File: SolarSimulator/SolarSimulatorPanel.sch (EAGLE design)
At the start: 82 parts, among them U1 Red Driver, U2 LM3404HVMA, U3 Blue Driver, X1 MKDSN1,5/2-5,08

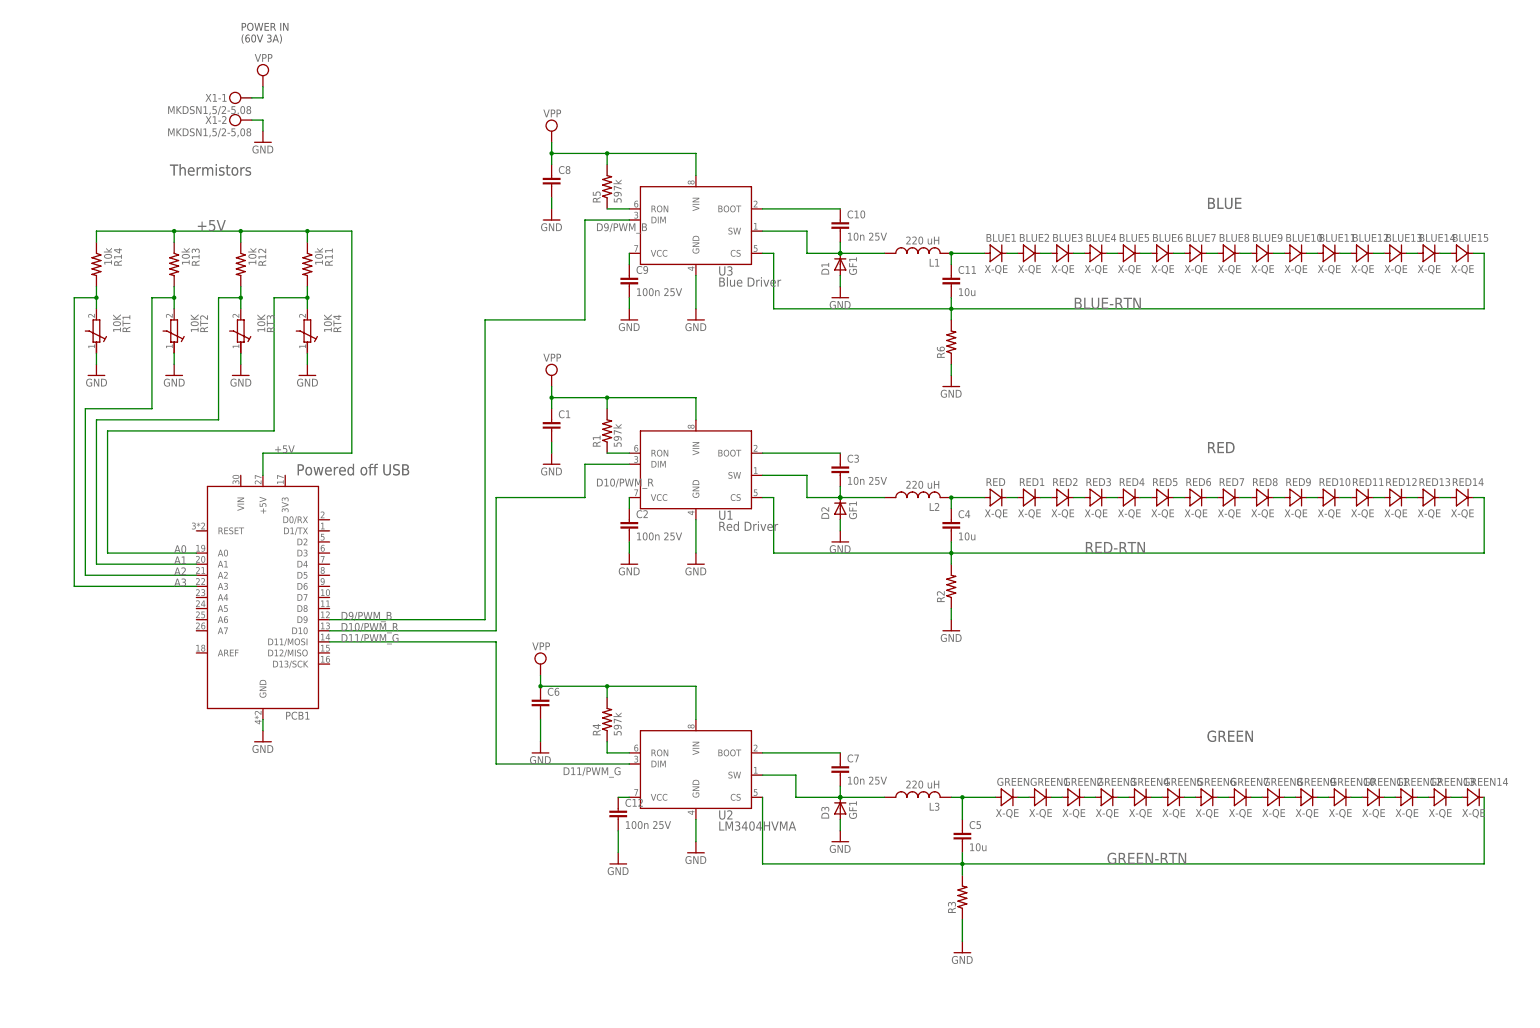
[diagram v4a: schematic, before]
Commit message: added BOM and cleaned up schematic a bit
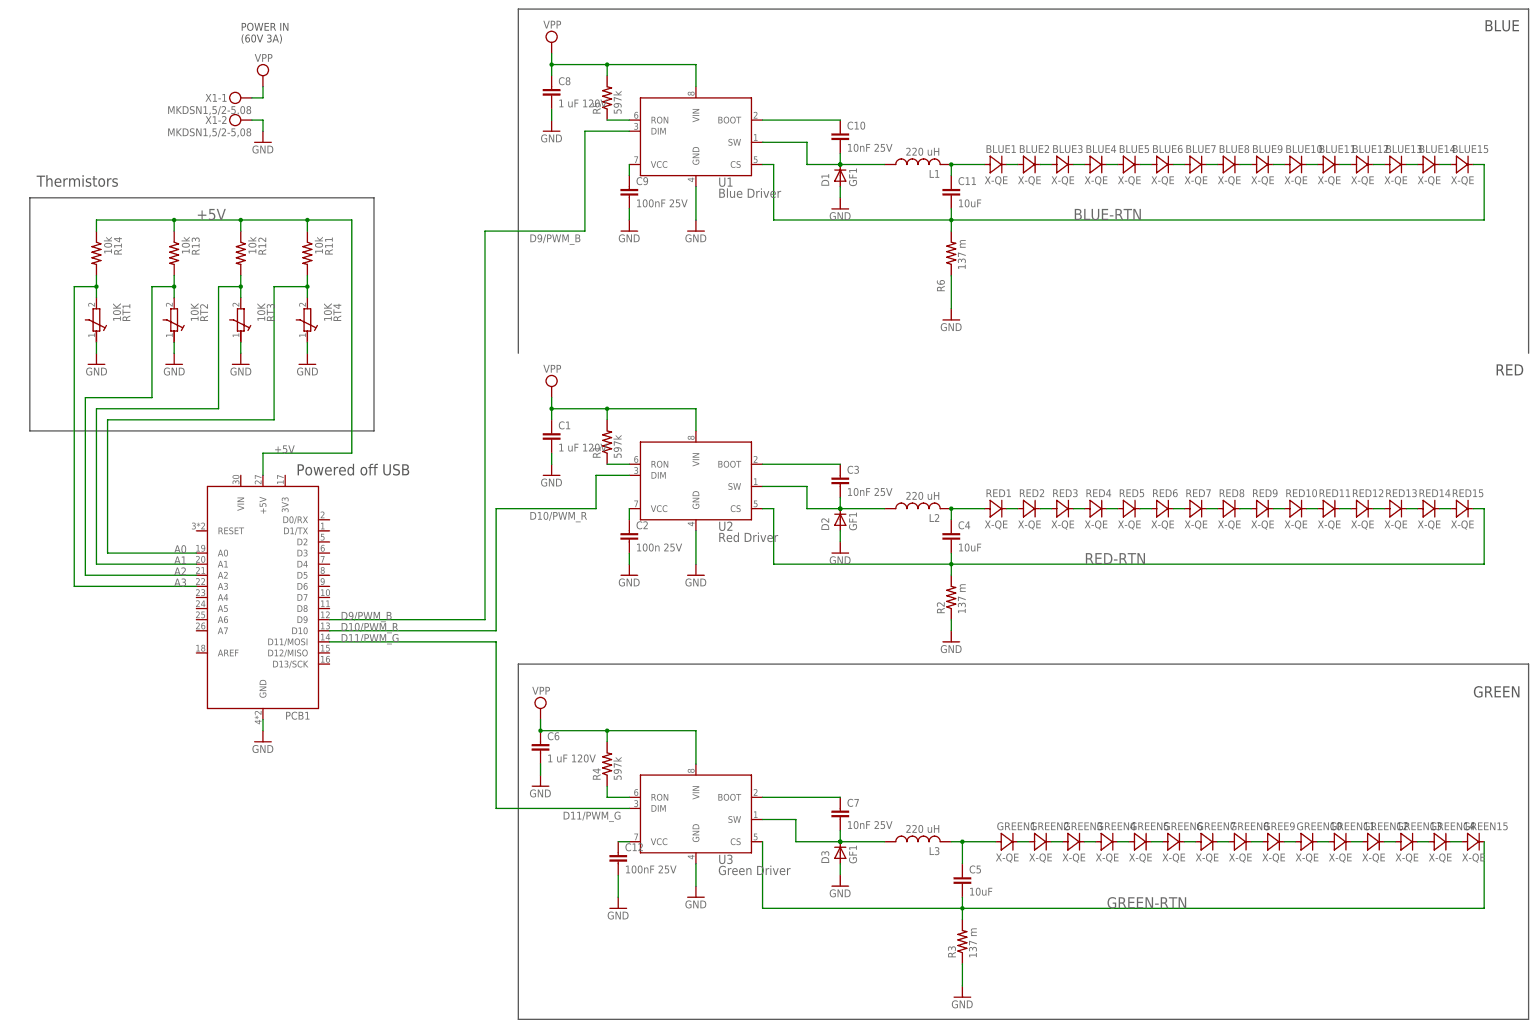
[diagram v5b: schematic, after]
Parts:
- removed GREEN, GREEN9, RED: X-QE, solarsim:X-QE
- added GREE9, GREEN15, RED15: X-QE, solarsim:X-QE
- C1, C6, C8: value (none) -> 1 uF 120V
- C10, C3, C7: value 10n 25V -> 10nF 25V
- C11, C4, C5: value 10u -> 10uF
- C12, C9: value 100n 25V -> 100nF 25V
- R2, R3, R6: value (none) -> 137 m
- U1: value Red Driver -> Blue Driver
- U2: value LM3404HVMA -> Red Driver
- U3: value Blue Driver -> Green Driver
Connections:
- removed net N$14 (its old number): RED.C, RED1.A
- removed net N$2 (its old number): GREEN10.A, GREEN9.C
- removed net N$35 (its old number): GREEN.C, GREEN1.A
- removed net N$5 (its old number): RED5.C, RED6.A
- new net N$13: RED14.C, RED15.A
- new net N$17: RED4.C, RED5.A
- new net N$41: GREE9.A, GREEN8.C
- new net N$46: GREEN14.C, GREEN15.A
- net 88: now also RED5.C, RED6.A; no longer RED4.C, RED5.A
- net BLUE-RTN: now also U1.CS; no longer U3.CS
- net D10/PWM_R: now also U2.DIM; no longer U1.DIM
- net D11/PWM_G: now also U3.DIM; no longer U2.DIM
- net D9/PWM_B: now also U1.DIM; no longer U3.DIM
- net GREEN-RTN: now also GREEN15.C, U3.CS; no longer GREEN14.C, U2.CS
- net GRN-OUT: now also GREEN1.A; no longer GREEN.A
- net N$1: now also U3.SW; no longer U2.SW
- net N$18: now also U1.RON; no longer U3.RON
- net N$19: now also U3.RON; no longer U2.RON
- net N$22: now also U2.BOOT; no longer U1.BOOT
- net N$25: now also U2.SW; no longer U1.SW
- net N$32: now also U3.BOOT; no longer U2.BOOT
- net N$33: now also U3.VCC; no longer U2.VCC
- net N$34: now also U1.SW; no longer U3.SW
- net N$4: now also U2.VCC; no longer U1.VCC
- net N$42: now also GREE9.C, GREEN10.A; no longer GREEN8.C, GREEN9.A
- net N$52: now also U1.BOOT; no longer U3.BOOT
- net N$53: now also U1.VCC; no longer U3.VCC
- net N$6: now also U2.RON; no longer U1.RON
- net RED-OUT: now also RED1.A; no longer RED.A
- net RED-RTN: now also RED15.C, U2.CS; no longer RED14.C, U1.CS
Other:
- moved on the sheet: BLUE1, BLUE10, BLUE11, BLUE12, BLUE13, BLUE14, BLUE15, BLUE2, BLUE3, BLUE4, BLUE5, BLUE6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

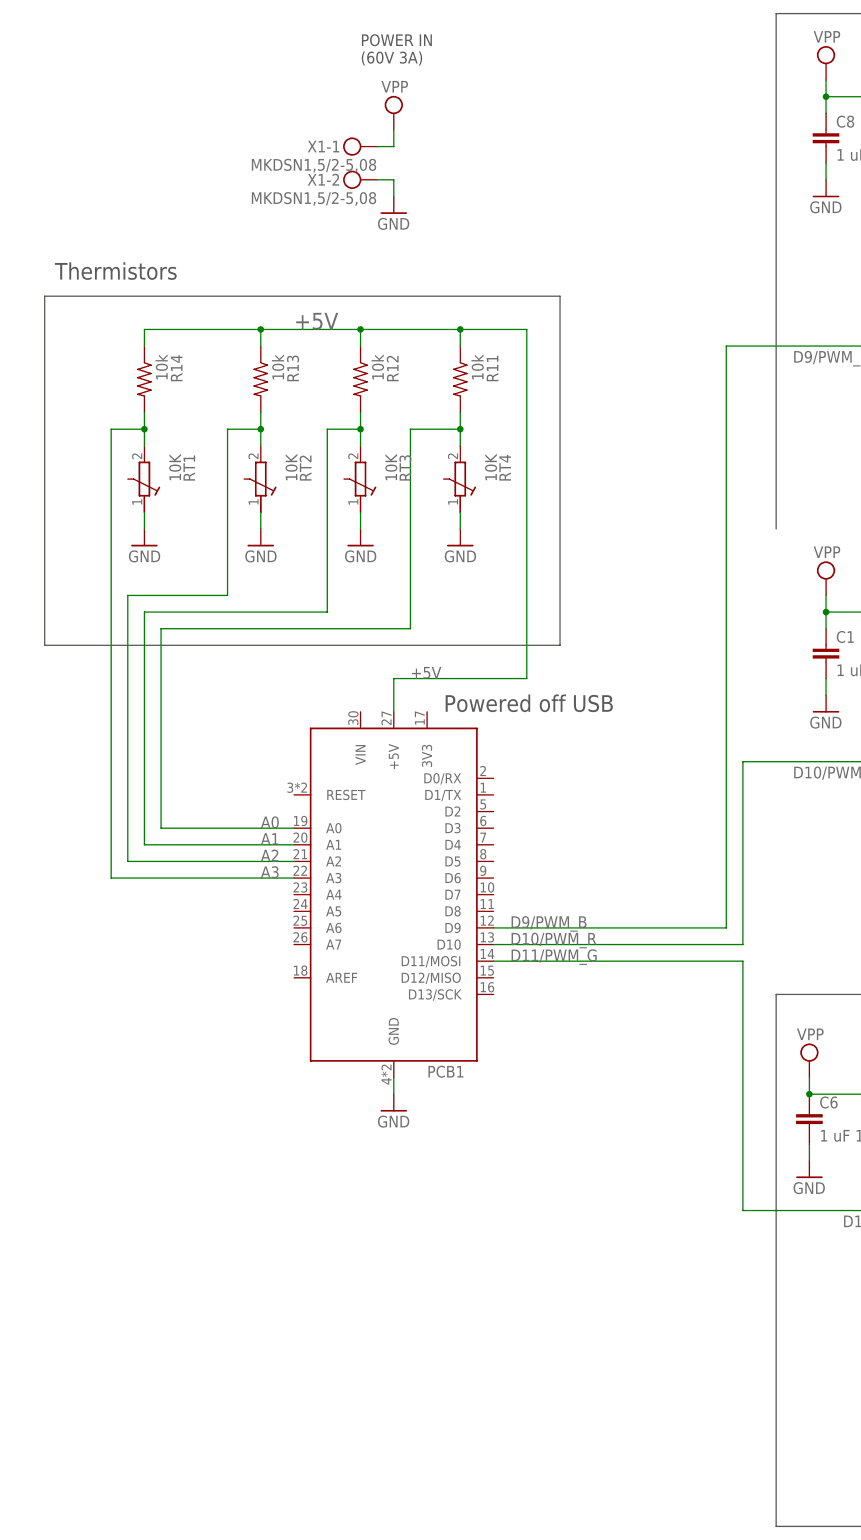
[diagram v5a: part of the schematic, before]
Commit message: combined/condensed needed libaries into a single library
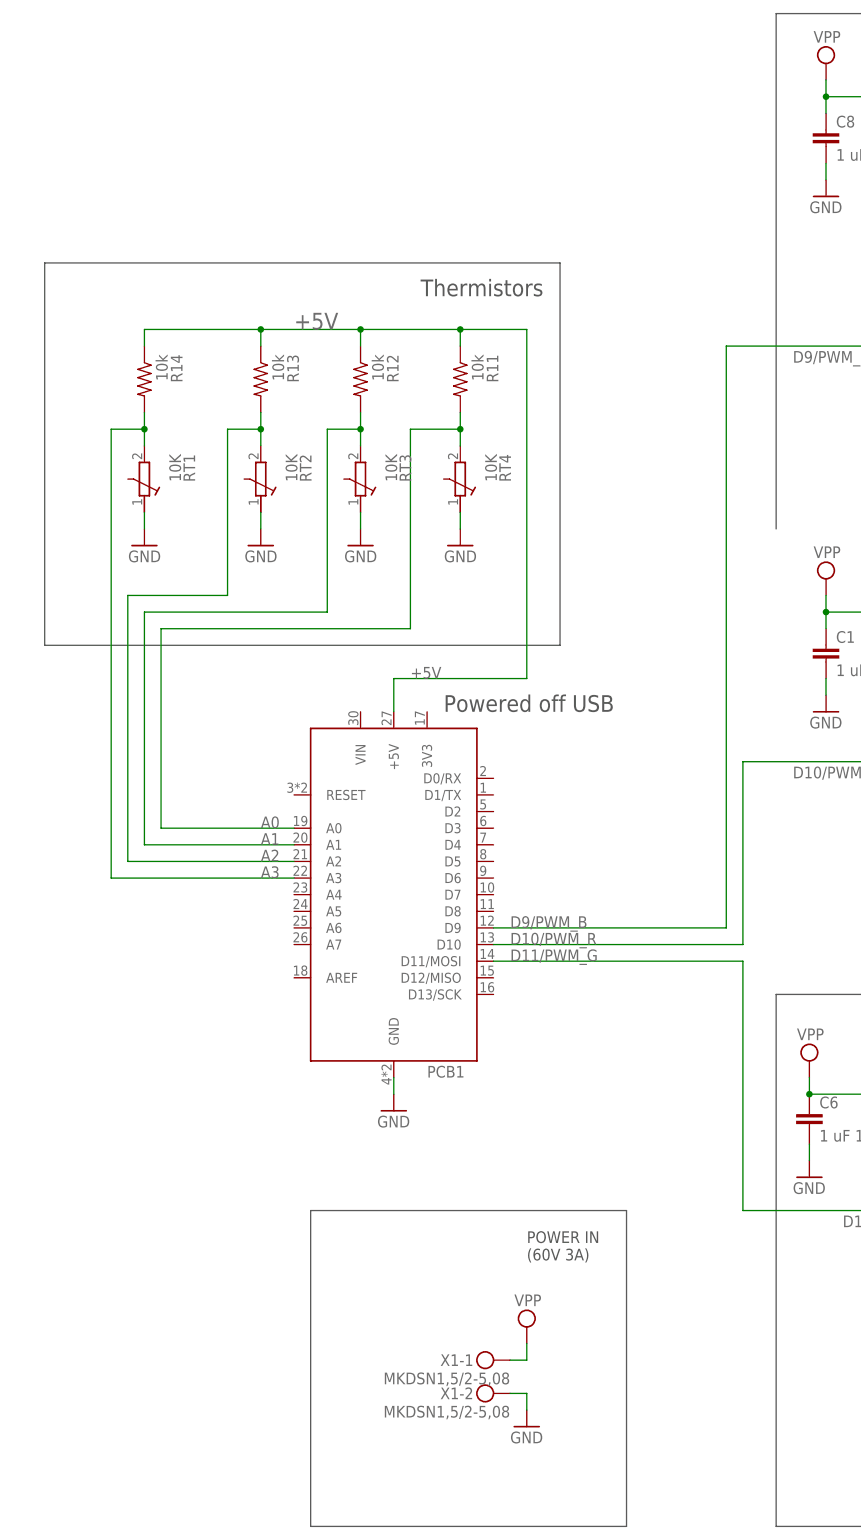
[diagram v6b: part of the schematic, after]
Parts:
- PCB1: device ARDUINO_NANO:ARDUINO_NANO -> solarsim:ARDUINO_NANO
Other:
- moved on the sheet: X1-1, X1-2
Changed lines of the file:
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@@
 <part name="GND20" library="supply1" library_urn="urn:adsk.eagle:library:371" deviceset="GND" device=""/>
 <part name="GND21" library="supply1" library_urn="urn:adsk.eagle:library:371" deviceset="GND" device=""/>
-<part name="PCB1" library="ARDUINO_NANO" deviceset="ARDUINO_NANO" device=""/>
+<part name="PCB1" library="solarsim" deviceset="ARDUINO_NANO" device=""/>
 </parts>
 <sheets>
 <sheet>
 <plain>
-<text x="101.6" y="261.62" size="1.778" layer="97">POWER IN
+<text x="127" y="78.74" size="1.778" layer="97">POWER IN
 (60V 3A)</text>
-<text x="73.66" y="231.14" size="2.54" layer="97" rot="R180">Thermistors</text>
+<text x="129.54" y="228.6" size="2.54" layer="97" rot="R180">Thermistors</text>
 <text x="383.54" y="111.76" size="2.54" layer="97">GREEN</text>
 <text x="388.62" y="185.42" size="2.54" layer="97">RED</text>
 <text x="386.08" y="264.16" size="2.54" layer="97">BLUE</text>
 <text x="114.3" y="162.56" size="2.54" layer="97">Powered off USB</text>
-<wire x1="53.34" y1="226.06" x2="53.34" y2="172.72" width="0.1524" layer="97"/>
+<wire x1="53.34" y1="231.14" x2="53.34" y2="172.72" width="0.1524" layer="97"/>
 <wire x1="53.34" y1="172.72" x2="132.08" y2="172.72" width="0.1524" layer="97"/>
-<wire x1="132.08" y1="172.72" x2="132.08" y2="226.06" width="0.1524" layer="97"/>
-<wire x1="132.08" y1="226.06" x2="53.34" y2="226.06" width="0.1524" layer="97"/>
+<wire x1="132.08" y1="172.72" x2="132.08" y2="231.14" width="0.1524" layer="97"/>
+<wire x1="132.08" y1="231.14" x2="53.34" y2="231.14" width="0.1524" layer="97"/>
 <wire x1="165.1" y1="119.38" x2="165.1" y2="38.1" width="0.1524" layer="97"/>
 <wire x1="165.1" y1="38.1" x2="396.24" y2="38.1" width="0.1524" layer="97"/>
@@
 <wire x1="165.1" y1="269.24" x2="396.24" y2="269.24" width="0.1524" layer="97"/>
 <wire x1="396.24" y1="269.24" x2="396.24" y2="190.5" width="0.1524" layer="97"/>
+<wire x1="93.98" y1="38.1" x2="142.24" y2="38.1" width="0.1524" layer="97"/>
+<wire x1="142.24" y1="38.1" x2="142.24" y2="86.36" width="0.1524" layer="97"/>
+<wire x1="142.24" y1="86.36" x2="93.98" y2="86.36" width="0.1524" layer="97"/>
+<wire x1="93.98" y1="86.36" x2="93.98" y2="38.1" width="0.1524" layer="97"/>
 </plain>
 <instances>
@@
 <attribute name="VALUE" x="236.22" y="142.24" size="1.778" layer="96"/>
 </instance>
-<instance part="X1" gate="-1" x="101.6" y="248.92" smashed="yes" rot="MR0">
-<attribute name="NAME" x="98.552" y="248.031" size="1.778" layer="95" rot="MR0"/>
-<attribute name="VALUE" x="104.14" y="245.237" size="1.778" layer="96" rot="MR0"/>
-</instance>
-<instance part="X1" gate="-2" x="101.6" y="243.84" smashed="yes" rot="MR0">
-<attribute name="NAME" x="98.552" y="242.951" size="1.778" layer="95" rot="MR0"/>
-<attribute name="VALUE" x="104.14" y="240.157" size="1.778" layer="96" rot="MR0"/>
-</instance>
-<instance part="GND10" gate="1" x="106.68" y="238.76" smashed="yes">
-<attribute name="VALUE" x="104.14" y="236.22" size="1.778" layer="96"/>
-</instance>
-<instance part="SUPPLY4" gate="G$1" x="106.68" y="254" smashed="yes">
-<attribute name="VALUE" x="104.775" y="257.175" size="1.778" layer="96"/>
+<instance part="X1" gate="-1" x="121.92" y="63.5" smashed="yes" rot="MR0">
+<attribute name="NAME" x="118.872" y="62.611" size="1.778" layer="95" rot="MR0"/>
+<attribute name="VALUE" x="124.46" y="59.817" size="1.778" layer="96" rot="MR0"/>
+</instance>
+<instance part="X1" gate="-2" x="121.92" y="58.42" smashed="yes" rot="MR0">
+<attribute name="NAME" x="118.872" y="57.531" size="1.778" layer="95" rot="MR0"/>
+<attribute name="VALUE" x="124.46" y="54.737" size="1.778" layer="96" rot="MR0"/>
+</instance>
+<instance part="GND10" gate="1" x="127" y="53.34" smashed="yes">
+<attribute name="VALUE" x="124.46" y="50.8" size="1.778" layer="96"/>
+</instance>
+<instance part="SUPPLY4" gate="G$1" x="127" y="68.58" smashed="yes">
+<attribute name="VALUE" x="125.095" y="71.755" size="1.778" layer="96"/>
 </instance>
 <instance part="C4" gate="CE" x="264.16" y="149.86" smashed="yes">
@@
 <segment>
 <pinref part="X1" gate="-2" pin="KL"/>
-<wire x1="104.14" y1="243.84" x2="106.68" y2="243.84" width="0.1524" layer="91"/>
+<wire x1="124.46" y1="58.42" x2="127" y2="58.42" width="0.1524" layer="91"/>
 <pinref part="GND10" gate="1" pin="GND"/>
-<wire x1="106.68" y1="243.84" x2="106.68" y2="241.3" width="0.1524" layer="91"/>
+<wire x1="127" y1="58.42" x2="127" y2="55.88" width="0.1524" layer="91"/>
 </segment>
 <segment>
@@
 </segment>
 <segment>
-<pinref part="PCB1" gate="G$1" pin="GND"/>
 <pinref part="GND18" gate="1" pin="GND"/>
 <wire x1="106.68" y1="104.14" x2="106.68" y2="106.68" width="0.1524" layer="91"/>
+<pinref part="PCB1" gate="G$1" pin="GND"/>
 </segment>
 </net>
@@
 <segment>
 <pinref part="X1" gate="-1" pin="KL"/>
-<wire x1="104.14" y1="248.92" x2="106.68" y2="248.92" width="0.1524" layer="91"/>
+<wire x1="124.46" y1="63.5" x2="127" y2="63.5" width="0.1524" layer="91"/>
 <pinref part="SUPPLY4" gate="G$1" pin="VPP"/>
-<wire x1="106.68" y1="248.92" x2="106.68" y2="251.46" width="0.1524" layer="91"/>
+<wire x1="127" y1="63.5" x2="127" y2="66.04" width="0.1524" layer="91"/>
 </segment>
 <segment>
@@
 <junction x="116.84" y="220.98"/>
 <label x="91.44" y="220.98" size="2.54" layer="95"/>
-<pinref part="PCB1" gate="G$1" pin="+5V"/>
 <wire x1="106.68" y1="162.56" x2="106.68" y2="167.64" width="0.1524" layer="91"/>
 <wire x1="106.68" y1="167.64" x2="127" y2="167.64" width="0.1524" layer="91"/>
 <label x="109.22" y="167.64" size="1.778" layer="95"/>
+<pinref part="PCB1" gate="G$1" pin="+5V"/>
 </segment>
 </net>
@@
 <wire x1="182.88" y1="162.56" x2="182.88" y2="154.94" width="0.1524" layer="91"/>
 <label x="167.64" y="152.4" size="1.778" layer="95"/>
-<pinref part="PCB1" gate="G$1" pin="D10"/>
 <wire x1="121.92" y1="127" x2="160.02" y2="127" width="0.1524" layer="91"/>
 <label x="124.46" y="127" size="1.778" layer="95"/>
 <wire x1="160.02" y1="127" x2="160.02" y2="154.94" width="0.1524" layer="91"/>
 <wire x1="160.02" y1="154.94" x2="182.88" y2="154.94" width="0.1524" layer="91"/>
+<pinref part="PCB1" gate="G$1" pin="D10"/>
 </segment>
 </net>
@@
 <label x="167.64" y="215.9" size="1.778" layer="95"/>
 <label x="124.46" y="129.54" size="1.778" layer="95"/>
-<pinref part="PCB1" gate="G$1" pin="D9"/>
 <pinref part="U1" gate="A" pin="DIM"/>
 <wire x1="190.5" y1="241.3" x2="180.34" y2="241.3" width="0.1524" layer="91"/>
 <wire x1="180.34" y1="218.44" x2="180.34" y2="241.3" width="0.1524" layer="91"/>
 <wire x1="180.34" y1="218.44" x2="157.48" y2="218.44" width="0.1524" layer="91"/>
+<pinref part="PCB1" gate="G$1" pin="D9"/>
 </segment>
 </net>
@@
 <wire x1="190.5" y1="86.36" x2="160.02" y2="86.36" width="0.1524" layer="91"/>
 <label x="175.26" y="83.82" size="1.778" layer="95"/>
-<wire x1="121.92" y1="124.46" x2="160.02" y2="124.46" width="0.1524" layer="91"/>
 <wire x1="160.02" y1="124.46" x2="160.02" y2="86.36" width="0.1524" layer="91"/>
 <label x="124.46" y="124.46" size="1.778" layer="95"/>
 <pinref part="PCB1" gate="G$1" pin="D11/MOSI"/>
-</segment>
-</net>
+<wire x1="160.02" y1="124.46" x2="121.92" y2="124.46" width="0.1524" layer="91"/>
+</segment>
+</net>
